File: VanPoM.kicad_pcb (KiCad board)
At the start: 2 copper layers, 5 parts, among them J1 Socket_ESP32-WROOM-32-NODEMCU, Q1 IPP055N03L G, Q2 IPP055N03L G, Q3 IPP120P04P4L03AKSA2, U1 BQ34Z100-R2

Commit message: +++ PCB; f many small things
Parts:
- added C1: 1000p, Capacitor_SMD:C_0603_1608Metric_Pad1.08x0.95mm_HandSolder, F.Cu at (140.3, 47.8)
- added C10: 1000p, Capacitor_SMD:C_0603_1608Metric_Pad1.08x0.95mm_HandSolder, F.Cu at (148.2, 53.1)
- added C11: 10u, Capacitor_SMD:C_1210_3225Metric_Pad1.33x2.70mm_HandSolder, F.Cu at (115.6, 70.0)
- added C12: 10u, Capacitor_SMD:C_1210_3225Metric_Pad1.33x2.70mm_HandSolder, F.Cu at (115.6, 74.3)
- added C13: 1000u, Capacitor_THT:CP_Radial_D16.0mm_P7.50mm, B.Cu at (115.8, 78.1)
- added C14: 0.1u, Capacitor_SMD:C_0603_1608Metric_Pad1.08x0.95mm_HandSolder, F.Cu at (109.3, 71.3)
- added C15: 1u, Capacitor_SMD:C_0402_1005Metric_Pad0.74x0.62mm_HandSolder, F.Cu at (111.3, 70.1)
- added C16: 0.1u, Capacitor_SMD:C_0603_1608Metric_Pad1.08x0.95mm_HandSolder, F.Cu at (105.2, 77.3)
- added C17: 0.1u, Capacitor_SMD:C_0603_1608Metric_Pad1.08x0.95mm_HandSolder, F.Cu at (173.4, 105.8)
- added C18: 0.1u, Capacitor_SMD:C_0603_1608Metric_Pad1.08x0.95mm_HandSolder, F.Cu at (173.4, 117.9)
- added C19: 1200u, Capacitor_THT:CP_Radial_D18.0mm_P7.50mm, B.Cu at (163.3, 89.8)
- added C2: 1u, Capacitor_SMD:C_0805_2012Metric_Pad1.18x1.45mm_HandSolder, F.Cu at (137.5, 96.9)
- added C20: 1200u, Capacitor_THT:CP_Radial_D18.0mm_P7.50mm, B.Cu at (178.7, 79.0)
- added C21: 0.1u, Capacitor_SMD:C_0603_1608Metric_Pad1.08x0.95mm_HandSolder, F.Cu at (173.4, 93.7)
- added C22: 4.7u, Capacitor_SMD:C_1206_3216Metric_Pad1.33x1.80mm_HandSolder, F.Cu at (179.7, 65.5)
- added C23: 4.7u, Capacitor_SMD:C_1206_3216Metric_Pad1.33x1.80mm_HandSolder, F.Cu at (179.7, 63.0)
- added C24: 4.7u, Capacitor_SMD:C_1206_3216Metric_Pad1.33x1.80mm_HandSolder, F.Cu at (179.7, 60.4)
- added C25: 4.7u, Capacitor_SMD:C_1206_3216Metric_Pad1.33x1.80mm_HandSolder, F.Cu at (179.7, 55.4)
- added C26: 4.7u, Capacitor_SMD:C_1206_3216Metric_Pad1.33x1.80mm_HandSolder, F.Cu at (179.7, 57.9)
- added C27: 10u, Capacitor_SMD:C_1210_3225Metric_Pad1.33x2.70mm_HandSolder, B.Cu at (177.5, 51.3)
- added C28: 0.022u, Capacitor_SMD:C_1206_3216Metric_Pad1.33x1.80mm_HandSolder, B.Cu at (187.9, 50.1)
- added C29: 50n, Capacitor_SMD:C_0402_1005Metric_Pad0.74x0.62mm_HandSolder, F.Cu at (185.4, 51.6)
- added C3: 220p, Capacitor_SMD:C_0603_1608Metric_Pad1.08x0.95mm_HandSolder, F.Cu at (142.9, 98.0)
- added C30: 10n, Capacitor_SMD:C_0402_1005Metric_Pad0.74x0.62mm_HandSolder, F.Cu at (183.2, 63.6)
- added C31: 1u, Capacitor_SMD:C_0805_2012Metric_Pad1.18x1.45mm_HandSolder, F.Cu at (143.2, 102.5)
- added C32: 1u, Capacitor_SMD:C_0402_1005Metric_Pad0.74x0.62mm_HandSolder, F.Cu at (143.9, 105.4)
- added C33: 0.1u, Capacitor_SMD:C_0603_1608Metric_Pad1.08x0.95mm_HandSolder, F.Cu at (180.4, 133.8)
- added C34: 0.1u, Capacitor_SMD:C_0603_1608Metric_Pad1.08x0.95mm_HandSolder, F.Cu at (128.5, 78.8)
- added C35: 0.1u, Capacitor_SMD:C_0603_1608Metric_Pad1.08x0.95mm_HandSolder, B.Cu at (109.3, 67.1)
- added C36: 0.1u, Capacitor_SMD:C_0603_1608Metric_Pad1.08x0.95mm_HandSolder, F.Cu at (137.9, 122.2)
- added C37: 0.1u, Capacitor_SMD:C_0603_1608Metric_Pad1.08x0.95mm_HandSolder, F.Cu at (145.0, 125.2)
- added C38: 0.1u, Capacitor_SMD:C_0603_1608Metric_Pad1.08x0.95mm_HandSolder, F.Cu at (148.1, 121.6)
- added C39: 0.1u, Capacitor_SMD:C_0603_1608Metric_Pad1.08x0.95mm_HandSolder, F.Cu at (147.5, 123.1)
- added C4: 560p, Capacitor_SMD:C_0402_1005Metric_Pad0.74x0.62mm_HandSolder, F.Cu at (140.0, 98.0)
- added C40: 0.1u, Capacitor_SMD:C_0603_1608Metric_Pad1.08x0.95mm_HandSolder, F.Cu at (141.6, 126.5)
- added C41: 0.1u, Capacitor_SMD:C_0603_1608Metric_Pad1.08x0.95mm_HandSolder, F.Cu at (140.1, 125.4)
- added C42: 0.1u, Capacitor_SMD:C_0603_1608Metric_Pad1.08x0.95mm_HandSolder, F.Cu at (136.4, 120.7)
- added C43: 0.1u, Capacitor_SMD:C_0603_1608Metric_Pad1.08x0.95mm_HandSolder, F.Cu at (143.1, 126.5)
- added C44: 1u, Capacitor_SMD:C_0402_1005Metric_Pad0.74x0.62mm_HandSolder, F.Cu at (143.5, 118.6)
- added C45: 1u, Capacitor_SMD:C_0402_1005Metric_Pad0.74x0.62mm_HandSolder, F.Cu at (145.2, 119.2)
- added C46: 1u, Capacitor_SMD:C_0402_1005Metric_Pad0.74x0.62mm_HandSolder, F.Cu at (147.0, 120.2)
- added C5: 0.1u, Capacitor_SMD:C_0603_1608Metric_Pad1.08x0.95mm_HandSolder, F.Cu at (140.6, 88.9)
- added C6: 0.1u, Capacitor_SMD:C_0603_1608Metric_Pad1.08x0.95mm_HandSolder, F.Cu at (150.7, 88.9)
- added C7: 560p, Capacitor_SMD:C_0402_1005Metric_Pad0.74x0.62mm_HandSolder, F.Cu at (149.0, 97.7)
- added C8: 220p, Capacitor_SMD:C_0603_1608Metric_Pad1.08x0.95mm_HandSolder, F.Cu at (151.9, 98.1)
- added C9: 1u, Capacitor_SMD:C_0805_2012Metric_Pad1.18x1.45mm_HandSolder, F.Cu at (146.5, 95.9)
- added D1: B1100-13-F, Diode_SMD:D_SMA, F.Cu at (142.7, 82.3)
- added D10: PESD2USB3UXT-QR, Package_TO_SOT_SMD:SOT-23-3, B.Cu at (105.8, 133.0)
- added D11: PESD2USB3UXT-QR, Package_TO_SOT_SMD:SOT-23-3, B.Cu at (105.9, 102.5)
- added D12: PESD2USB3UXT-QR, Package_TO_SOT_SMD:SOT-23-3, B.Cu at (105.8, 127.9)
- added D13: PESD2USB3UXT-QR, Package_TO_SOT_SMD:SOT-23-3, B.Cu at (105.9, 97.5)
- added D14: PESD2USB3UXT-QR, Package_TO_SOT_SMD:SOT-23-3, B.Cu at (105.9, 122.9)
- added D15: PESD2USB3UXT-QR, Package_TO_SOT_SMD:SOT-23-3, B.Cu at (105.8, 92.4)
- added D16: PESD2USB3UXT-QR, Package_TO_SOT_SMD:SOT-23-3, B.Cu at (105.8, 117.8)
- added D17: PESD2USB3UXT-QR, Package_TO_SOT_SMD:SOT-23-3, B.Cu at (105.9, 87.3)
- added D18: PESD2USB3UXT-QR, Package_TO_SOT_SMD:SOT-23-3, B.Cu at (105.8, 112.7)
- added D2: D, Diode_SMD:D_SMA, F.Cu at (136.6, 91.0)
- added D21: PESD2USB3UXT-QR, Package_TO_SOT_SMD:SOT-23-3, B.Cu at (110.0, 115.2)
- added D22: PESD2USB3UXT-QR, Package_TO_SOT_SMD:SOT-23-3, B.Cu at (110.0, 120.3)
- added D23: PESD2USB3UXT-QR, Package_TO_SOT_SMD:SOT-23-3, B.Cu at (110.0, 125.5)
- added D24: PESD2USB3UXT-QR, Package_TO_SOT_SMD:SOT-23-3, B.Cu at (110.0, 130.5)
- added D25: PESD2USB3UXT-QR, Package_TO_SOT_SMD:SOT-23-3, B.Cu at (110.0, 136.1)
- added D3: D, Diode_SMD:D_SMA, F.Cu at (146.3, 90.8)
- added D4: B1100-13-F, Diode_SMD:D_SMA, F.Cu at (150.6, 82.3)
- added D5: BZT52C15-7-F, Diode_SMD:D_SOD-123, F.Cu at (97.1, 71.6)
- added D6: PESD2USB3UXT-QR, Package_TO_SOT_SMD:SOT-23-3, B.Cu at (97.7, 78.2)
- added D7: PESD2USB3UXT-QR, Package_TO_SOT_SMD:SOT-23-3, B.Cu at (101.5, 79.1)
- added D8: PESD2USB3UXT-QR, Package_TO_SOT_SMD:SOT-23-3, B.Cu at (105.8, 138.1)
- added D9: PESD2USB3UXT-QR, Package_TO_SOT_SMD:SOT-23-3, B.Cu at (105.9, 107.6)
- added FB1: 74279201, Capacitor_SMD:C_0805_2012Metric_Pad1.18x1.45mm_HandSolder, F.Cu at (180.4, 137.7)
- added FB2: 74279201, Capacitor_SMD:C_0805_2012Metric_Pad1.18x1.45mm_HandSolder, F.Cu at (132.5, 78.8)
- added FB3: 74279201, Capacitor_SMD:C_0805_2012Metric_Pad1.18x1.45mm_HandSolder, B.Cu at (111.2, 68.8)
- added IC1: UCC27517DBVR, Perso:SOT95P280X145-5N, F.Cu at (105.2, 74.4)
- added IC2: TLV70433DBVT, Perso:SOT95P280X145-5N, F.Cu at (147.3, 104.1)
- added IC3: SN74LV4052APWR, Package_SO:TSSOP-16_4.4x5mm_P0.65mm, F.Cu at (119.0, 133.3)
- added J10: UART1, Connector_PinHeader_2.54mm:PinHeader_1x04_P2.54mm_Vertical, B.Cu at (121.5, 128.3)
- added J11: I2C, Connector_PinHeader_2.54mm:PinHeader_1x04_P2.54mm_Vertical, B.Cu at (121.5, 138.0)
- added J2: OSTT7020150, TerminalBlock_MetzConnect:TerminalBlock_MetzConnect_Type073_RT02602HBLU_1x02_P5.08mm_Horizontal, B.Cu at (185.6, 123.8)
- added J3: OSTT7020150, TerminalBlock_MetzConnect:TerminalBlock_MetzConnect_Type073_RT02602HBLU_1x02_P5.08mm_Horizontal, B.Cu at (185.6, 99.7)
- added J4: OSTT7020150, TerminalBlock_MetzConnect:TerminalBlock_MetzConnect_Type073_RT02602HBLU_1x02_P5.08mm_Horizontal, B.Cu at (110.1, 51.4)
- added J5: OSTT7020150, TerminalBlock_MetzConnect:TerminalBlock_MetzConnect_Type073_RT02602HBLU_1x02_P5.08mm_Horizontal, B.Cu at (98.0, 51.4)
- added J6: Conn_03x23_Row_Letter_First, Perso:PinHeader_3x23_P2.54mm_Vertical, B.Cu at (101.8, 83.2)
- added J7: UART4, Connector_PinHeader_2.54mm:PinHeader_1x04_P2.54mm_Vertical, B.Cu at (121.5, 111.1)
- added J8: UART3, Connector_PinHeader_2.54mm:PinHeader_1x04_P2.54mm_Vertical, B.Cu at (121.5, 116.8)
- added J9: UART2, Connector_PinHeader_2.54mm:PinHeader_1x04_P2.54mm_Vertical, B.Cu at (121.5, 122.5)
- added L1: 22u, Inductor_SMD:L_Wuerth_HCF-2818, F.Cu at (128.7, 62.9)
- added L2: 22u, Inductor_SMD:L_Wuerth_HCF-2818, F.Cu at (166.6, 62.9)
- added L3: 220u, Perso:INDPM105103X500N, B.Cu at (185.4, 58.7)
- added Q10: CSD18540Q5B, Package_SON:VSONP-8-1EP_5x6_P1.27mm, F.Cu at (167.4, 123.2)
- added Q11: CSD18540Q5B, Package_SON:VSONP-8-1EP_5x6_P1.27mm, F.Cu at (167.4, 99.1)
- added Q4: CSD19531Q5A, Package_SON:VSONP-8-1EP_5x6_P1.27mm, F.Cu at (152.8, 76.7)
- added Q5: NX7002AK,215, Package_TO_SOT_SMD:SOT-23-3, F.Cu at (115.3, 63.4)
- added Q6: BSS84W-7-F, Package_TO_SOT_SMD:SOT-323_SC-70_Handsoldering, F.Cu at (114.7, 57.2)
- added Q7: CSD18540Q5B, Package_SON:VSONP-8-1EP_5x6_P1.27mm, F.Cu at (101.9, 67.9)
- added Q8: CSD18540Q5B, Package_SON:VSONP-8-1EP_5x6_P1.27mm, F.Cu at (98.4, 57.1)
- added Q9: CSD18540Q5B, Package_SON:VSONP-8-1EP_5x6_P1.27mm, F.Cu at (167.4, 111.1)
- added R1: 5.6, Resistor_SMD:R_0805_2012Metric_Pad1.20x1.40mm_HandSolder, F.Cu at (140.1, 51.8)
- added R10: 330k, Resistor_SMD:R_0805_2012Metric_Pad1.20x1.40mm_HandSolder, F.Cu at (115.4, 60.3)
- added R11: 390k, Resistor_SMD:R_0805_2012Metric_Pad1.20x1.40mm_HandSolder, F.Cu at (112.1, 63.6)
- added R12: 30k, Resistor_SMD:R_0805_2012Metric_Pad1.20x1.40mm_HandSolder, F.Cu at (112.1, 67.4)
- added R13: 10k, Resistor_SMD:R_0805_2012Metric_Pad1.20x1.40mm_HandSolder, F.Cu at (98.1, 75.3)
- added R14: 5.11, Resistor_SMD:R_0805_2012Metric_Pad1.20x1.40mm_HandSolder, F.Cu at (101.4, 73.2)
- added R15: 100k, Resistor_SMD:R_0805_2012Metric_Pad1.20x1.40mm_HandSolder, F.Cu at (176.1, 105.7)
- added R16: 100k, Resistor_SMD:R_0805_2012Metric_Pad1.20x1.40mm_HandSolder, F.Cu at (176.1, 117.7)
- added R17: 140k, Resistor_SMD:R_0805_2012Metric_Pad1.20x1.40mm_HandSolder, B.Cu at (177.0, 47.4)
- added R18: 220k, Resistor_SMD:R_0805_2012Metric_Pad1.20x1.40mm_HandSolder, F.Cu at (183.6, 56.4)
- added R19: 30k, Resistor_SMD:R_0805_2012Metric_Pad1.20x1.40mm_HandSolder, F.Cu at (182.6, 53.1)
- added R2: 4.42, Resistor_SMD:R_0805_2012Metric_Pad1.20x1.40mm_HandSolder, F.Cu at (142.8, 86.1)
- added R20: 3.00, Resistor_SMD:R_0805_2012Metric_Pad1.20x1.40mm_HandSolder, F.Cu at (183.6, 60.6)
- added R21: 10k, Resistor_SMD:R_0805_2012Metric_Pad1.20x1.40mm_HandSolder, F.Cu at (139.1, 114.7)
- added R22: 10k, Resistor_SMD:R_0805_2012Metric_Pad1.20x1.40mm_HandSolder, F.Cu at (139.1, 116.8)
- added R23: 100k, Resistor_SMD:R_0805_2012Metric_Pad1.20x1.40mm_HandSolder, F.Cu at (152.4, 138.9)
- added R24: 1.8M, Resistor_SMD:R_0805_2012Metric_Pad1.20x1.40mm_HandSolder, F.Cu at (148.9, 128.0)
- added R25: 1.8M, Resistor_SMD:R_0805_2012Metric_Pad1.20x1.40mm_HandSolder, F.Cu at (150.8, 120.9)
- added R26: 1.8M, Resistor_SMD:R_0805_2012Metric_Pad1.20x1.40mm_HandSolder, F.Cu at (146.9, 131.1)
- added R27: 1.8M, Resistor_SMD:R_0805_2012Metric_Pad1.20x1.40mm_HandSolder, F.Cu at (137.1, 125.4)
- added R28: 200k, Resistor_SMD:R_0805_2012Metric_Pad1.20x1.40mm_HandSolder, F.Cu at (135.2, 123.4)
- added R29: 200k, Resistor_SMD:R_0805_2012Metric_Pad1.20x1.40mm_HandSolder, F.Cu at (146.1, 128.0)
- added R3: 2.21, Resistor_SMD:R_0805_2012Metric_Pad1.20x1.40mm_HandSolder, F.Cu at (140.6, 73.7)
- added R30: 200k, Resistor_SMD:R_0805_2012Metric_Pad1.20x1.40mm_HandSolder, F.Cu at (150.8, 117.1)
- added R31: 200k, Resistor_SMD:R_0805_2012Metric_Pad1.20x1.40mm_HandSolder, F.Cu at (149.7, 125.0)
- added R32: R, Resistor_SMD:R_0805_2012Metric_Pad1.20x1.40mm_HandSolder, F.Cu at (146.9, 117.6)
- added R33: R, Resistor_SMD:R_0805_2012Metric_Pad1.20x1.40mm_HandSolder, F.Cu at (143.1, 117.1)
- added R34: 100k, Resistor_SMD:R_0805_2012Metric_Pad1.20x1.40mm_HandSolder, B.Cu at (117.6, 125.3)
- added R35: 100k, Resistor_SMD:R_0805_2012Metric_Pad1.20x1.40mm_HandSolder, B.Cu at (117.7, 113.9)
- added R36: 100k, Resistor_SMD:R_0805_2012Metric_Pad1.20x1.40mm_HandSolder, B.Cu at (117.7, 108.2)
- added R37: 100k, Resistor_SMD:R_0805_2012Metric_Pad1.20x1.40mm_HandSolder, B.Cu at (117.6, 119.6)
- added R4: 2.21, Resistor_SMD:R_0805_2012Metric_Pad1.20x1.40mm_HandSolder, F.Cu at (146.8, 62.7)
- added R5: 2.21, Resistor_SMD:R_0805_2012Metric_Pad1.20x1.40mm_HandSolder, F.Cu at (158.6, 82.8)
- added R6: 2.21, Resistor_SMD:R_0805_2012Metric_Pad1.20x1.40mm_HandSolder, F.Cu at (148.9, 73.6)
- added R7: 4.42, Resistor_SMD:R_0805_2012Metric_Pad1.20x1.40mm_HandSolder, F.Cu at (152.8, 86.2)
- added R8: 5.6, Resistor_SMD:R_0805_2012Metric_Pad1.20x1.40mm_HandSolder, F.Cu at (148.1, 56.9)
- added R9: 240k, Resistor_SMD:R_0805_2012Metric_Pad1.20x1.40mm_HandSolder, F.Cu at (115.7, 54.5)
- added R_sense1: 2m, Perso:R_Shunt_Ohmite_LVK25-fixed, F.Cu at (120.9, 84.2)
- added R_sense2: 2m, Perso:R_Shunt_Ohmite_LVK25-fixed, F.Cu at (109.3, 57.3)
- added R_sense3: 2m, Perso:R_Shunt_Ohmite_LVK25-fixed, F.Cu at (175.3, 126.2)
- added U10: LM5163DDAR, Perso:SOIC-8-1EP_3.9x4.9mm_P1.27mm_EP2.34x2.34mm_ThermalVias, B.Cu at (182.9, 49.7)
- added U11: TVS3300DRV, Package_SON:WSON-6-1EP_2x2mm_P0.65mm_EP1x1.6mm, B.Cu at (103.3, 58.9)
- added U12: TVS3300DRV, Package_SON:WSON-6-1EP_2x2mm_P0.65mm_EP1x1.6mm, B.Cu at (121.1, 49.7)
- added U13: ESP32-S3-DEVKITC-1-N16R2, Perso:XCVR_ESP32-S3-DEVKITC-1, B.Cu at (144.4, 110.4)
- added U14: INA240A2D, Package_SO:SOIC-8_3.9x4.9mm_P1.27mm, F.Cu at (175.4, 133.9)
- added U15: INA240A2D, Package_SO:SOIC-8_3.9x4.9mm_P1.27mm, F.Cu at (128.6, 84.2)
- added U16: INA240A2D, Package_SO:SOIC-8_3.9x4.9mm_P1.27mm, B.Cu at (109.3, 63.6)
- added U17: TLA2528IRTER, Perso:WQFN16_RTE_TEX-L, F.Cu at (142.6, 121.0)
- added U18: TVS3300DRV, Package_SON:WSON-6-1EP_2x2mm_P0.65mm_EP1x1.6mm, B.Cu at (98.9, 58.9)
- added U2: LM5109BMA/NOPB, Package_SO:SOIC-8_3.9x4.9mm_P1.27mm, F.Cu at (151.4, 93.3)
- added U3: BQ34Z100-R2, Package_SO:TSSOP-14_4.4x5mm_P0.65mm, F.Cu at (108.3, 65.7)
- added U4: TVS3300DRV, Package_SON:WSON-6-1EP_2x2mm_P0.65mm_EP1x1.6mm, B.Cu at (178.3, 111.7)
- added U5: TVS3300DRV, Package_SON:WSON-6-1EP_2x2mm_P0.65mm_EP1x1.6mm, B.Cu at (178.3, 123.8)
- added U6: LM74700, Package_TO_SOT_SMD:SOT-23-6, F.Cu at (170.3, 105.5)
- added U7: LM74700, Package_TO_SOT_SMD:SOT-23-6, F.Cu at (170.3, 117.6)
- added U8: LM74700, Package_TO_SOT_SMD:SOT-23-6, F.Cu at (170.3, 93.5)
- added U9: TVS3300DRV, Package_SON:WSON-6-1EP_2x2mm_P0.65mm_EP1x1.6mm, B.Cu at (185.8, 95.2)
- J1: value Socket_ESP32-WROOM-32-NODEMCU -> OSTT7020150; footprint Connector_PinSocket_2.54mm:PinSocket_1x19_P2.54mm_Vertical -> TerminalBlock_MetzConnect:TerminalBlock_MetzConnect_Type073_RT02602HBLU_1x02_P5.08mm_Horizontal; moved to B.Cu
- Q1, Q2: value IPP055N03L G -> CSD19531Q5A; footprint Package_TO_SOT_THT:TO-220-3_Vertical -> Package_SON:VSONP-8-1EP_5x6_P1.27mm
- Q3: value IPP120P04P4L03AKSA2 -> CSD19531Q5A; footprint Package_TO_SOT_THT:TO-220-3_Vertical -> Package_SON:VSONP-8-1EP_5x6_P1.27mm
- U1: value BQ34Z100-R2 -> LM5109BMA/NOPB; footprint Package_SO:TSSOP-14_4.4x5mm_P0.65mm -> Package_SO:SOIC-8_3.9x4.9mm_P1.27mm
- moved J1 67.3 mm to (185.6, 111.8), turned to -90 degrees
- moved Q3 52.7 mm to (152.7, 49.8), turned to 90 degrees
- moved Q2 44.0 mm to (144.3, 49.8), turned to 90 degrees
- moved Q1 17.3 mm to (144.9, 76.7), turned to 90 degrees
- moved U1 13.7 mm to (141.2, 93.3), turned to 90 degrees
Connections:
- J1 pad 1: unconnected-(J1-5V-Pad1) -> V_S
- J1 pad 2: unconnected-(J1-CLK-Pad2) -> P-
- Q1 pad 1: Net-(D1-K) -> P-
- Q1 pad 2: BAT + -> Net-(Q1-S-Pad2)
- Q1 pad 3: (no net) -> Net-(L1-Pad2)
- Q2 pad 1: BAT - -> Net-(L1-Pad2)
- Q2 pad 3: (no net) -> V_IN
- Q3 pad 3: BAT + -> V_IN
- U1 pad 1: BAT - -> +10V
- U1 pad 2: Net-(Q2-G) -> PW_H1
- U1 pad 3: BAT - -> PW_L1
- U1 pad 4: Net-(U1-BAT) -> P-
- U1 pad 5: Net-(Q1-3) -> Net-(U1-LO)
- U1 pad 6: Net-(Q1-3) -> Net-(D1-K)
- U1 pad 7: unconnected-(U1-REG25-Pad7) -> Net-(U1-HO)
- U1 pad 8: BAT - -> Net-(D2-K)
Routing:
- net P-: track 0.00 -> 606.7 mm, vias 0 -> 189
- net +3V3: track 0.00 -> 372.3 mm, vias 0 -> 8
- net TVS: track 0.00 -> 222.3 mm, vias 0 -> 2
- net 103AT: track 0.00 -> 158.9 mm
- net +10V: track 0.00 -> 146.1 mm, vias 0 -> 8
- net SCL: track 0.00 -> 139.4 mm, vias 0 -> 5
- net SDA: track 0.00 -> 132.7 mm, vias 0 -> 2
- net GPIO19: track 0.00 -> 93.1 mm
- net AIO_2: track 0.00 -> 91.1 mm, vias 0 -> 3
- net GPIO39: track 0.00 -> 88.7 mm, vias 0 -> 2
- net GPIO20: track 0.00 -> 87.1 mm
- net GPIO40: track 0.00 -> 86.8 mm, vias 0 -> 2
- net TVS_3v3: track 0.00 -> 86.3 mm
- net GPIO1: track 0.00 -> 86.2 mm, vias 0 -> 2
- net GPIO41: track 0.00 -> 85.7 mm, vias 0 -> 2
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- added copper zone on F.Cu, net +10V
- added copper zone on F.Cu, net +3V3
- added copper zone on B.Cu, net BAT+
- added copper zone on F.Cu, net BAT+
- added copper zone on F.Cu, net BAT-
- added copper zone on F.Cu, net Net-(C11-Pad1)
- added copper zone on F.Cu, net Net-(D2-K)
- added copper zone on F.Cu, net Net-(D3-K)
- added copper zone on B.Cu, net Net-(L1-Pad2)
- added copper zone on F.Cu, net Net-(L1-Pad2)
- added copper zone on B.Cu, net Net-(L2-Pad1)
- added copper zone on F.Cu, net Net-(L2-Pad1)
- added copper zone on F.Cu, net Net-(Q7-S-Pad3)
- added copper zone on B.Cu, net Net-(U10-SW)
- added copper zone on B.Cu, net OUT-
- added copper zone on F.Cu, net OUT-
- added copper zone on B.Cu, net P+
- added copper zone on F.Cu, net P+
- added copper zone on B.Cu, net P-
- added copper zone on F.Cu, net P-
- added copper zone on B.Cu, net V_A
- added copper zone on F.Cu, net V_A
- added copper zone on B.Cu, net V_IN
- added copper zone on F.Cu, net V_IN
- added copper zone on F.Cu, net V_P
- added copper zone on B.Cu, net V_S
- added copper zone on F.Cu, net V_S
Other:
- board outline added: 97 x 97 mm
- board text added: "+"
- board text added: "+15V INPUT (FROM AC/DC CONVERTER)"
- board text added: "00"
- board text added: "01"
- board text added: "02"
- board text added: "03"
- board text added: "06"
- board text added: "07"
- board text added: "08"
- board text added: "15"
- board text added: "16"
- board text added: "17"
- board text added: "18"
- board text added: "19"
- board text added: "20"
- board text added: "21"
- board text added: "39"
- board text added: "3V3"
- board text added: "40"
- board text added: "41"
- board text added: "42"
- board text added: "45"
- board text added: "46"
- board text added: "47"
- board text added: "48"
- board text added: "BAT TEMP"
- board text added: "BATTERY"
- board text added: "CAR BATTERY"
- board text added: "GND"
- board text added: "I2C"
- board text added: "IO"
- board text added: "LOAD"
- board text added: "RX"
- board text added: "SCL"
- board text added: "SDA"
- board text added: "SOLAR PANELS"
- board text added: "TX"
- board text added: "UART1"
- board text added: "UART2"
- board text added: "UART3"
- board text added: "UART4"
- board text added: "VanPom v1.0 Copyright © Léo Flaventin Hauchecorne https://github.com/hl037/VanPom"
- board text added: "−"

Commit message: + screen shots
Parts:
- moved C10 72.6 mm to (77.7, 36.0)
- moved C37 72.6 mm to (74.4, 108.1)
- moved C41 72.6 mm to (69.5, 108.4)
- moved C43 72.6 mm to (72.6, 109.4)
- moved C9 72.6 mm to (76.0, 78.8)
- moved L3 72.6 mm to (114.8, 41.6)
- moved R21 72.6 mm to (68.5, 97.6)
- moved R22 72.6 mm to (68.5, 99.7)
- moved R26 72.6 mm to (76.4, 114.0)
- moved R32 72.6 mm to (76.4, 100.5)
- moved R5 72.6 mm to (88.0, 65.7)
- moved U1 72.6 mm to (70.6, 76.3)
- moved U6 72.6 mm to (99.7, 88.4)
- moved U7 72.6 mm to (99.7, 100.5)
- moved U8 72.6 mm to (99.7, 76.4)
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
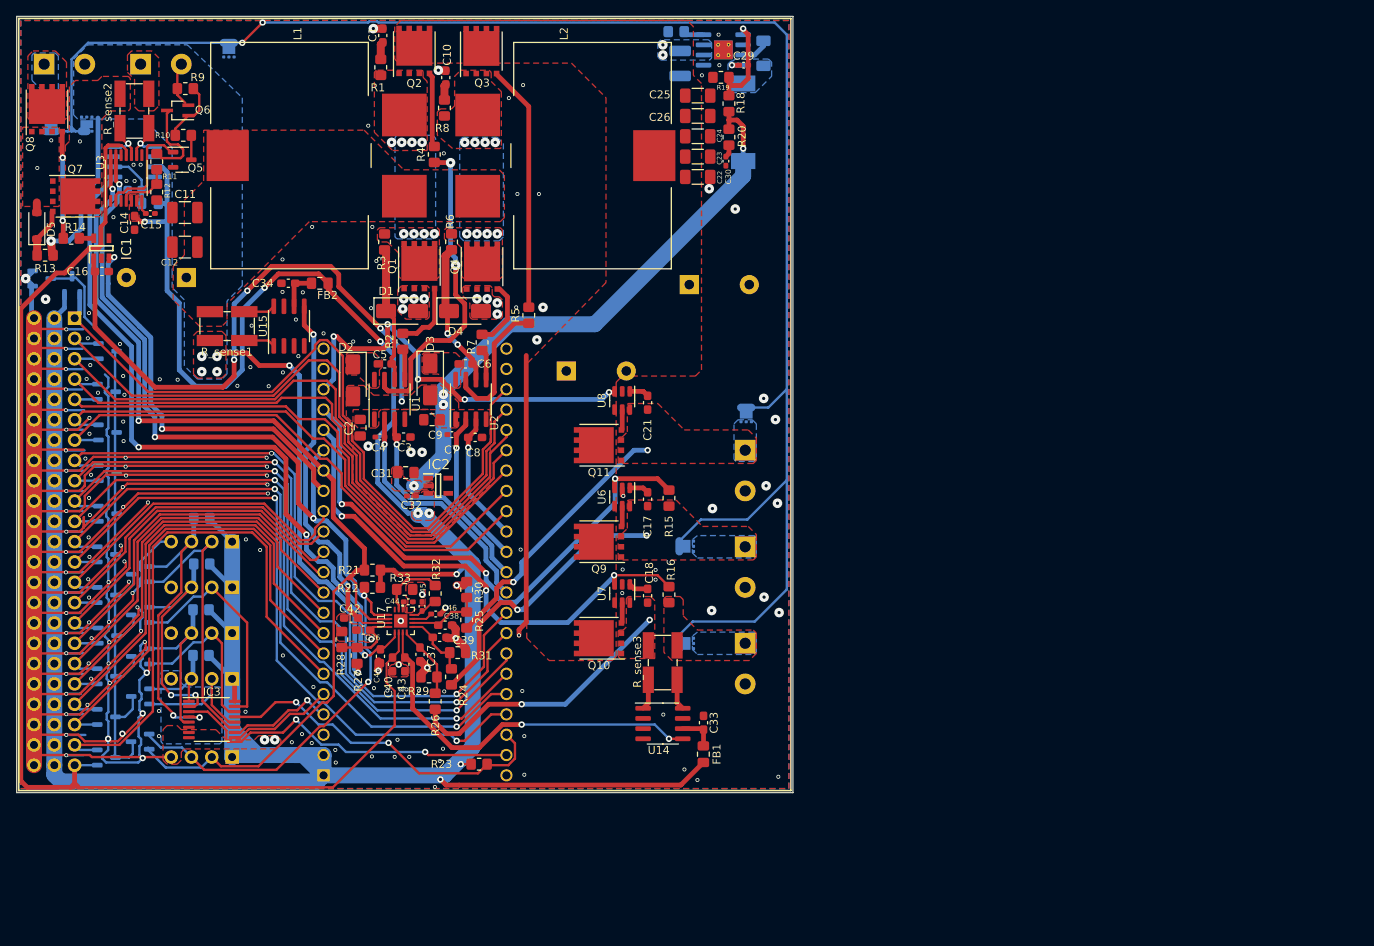
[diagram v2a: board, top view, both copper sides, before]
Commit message: + Thermal reliefs
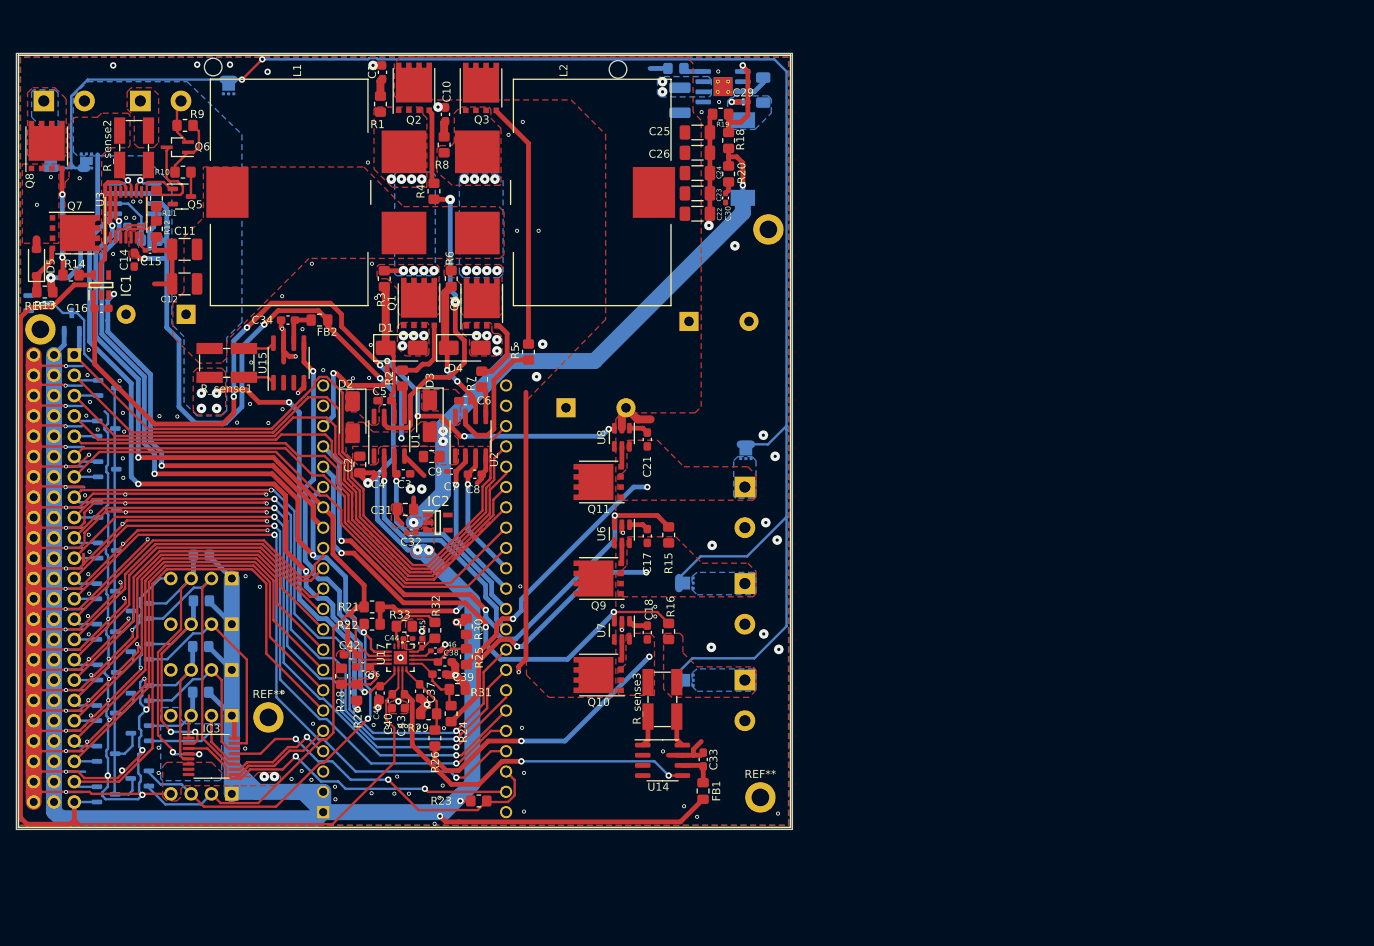
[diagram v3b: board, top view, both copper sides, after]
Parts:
- added ?: , , F.Cu at (118.0, 55.0)
- added REF**: MountingHole_2.2mm_M2_DIN965_Pad, MountingHole:MountingHole_2.2mm_M2_DIN965_Pad, F.Cu at (117.0, 126.0)
- added REF**: MountingHole_2.2mm_M2_DIN965_Pad, MountingHole:MountingHole_2.2mm_M2_DIN965_Pad, F.Cu at (55.5, 116.0)
- added REF**: MountingHole_2.2mm_M2_DIN965_Pad, MountingHole:MountingHole_2.2mm_M2_DIN965_Pad, F.Cu at (27.0, 67.5)
- moved D7 4.60 mm to (30.9, 66.6)
- moved Q4 4.60 mm to (82.2, 64.2)
- moved C1 4.60 mm to (69.8, 35.4)
- moved C12 4.60 mm to (45.0, 61.8)
- moved C13 4.60 mm to (45.2, 65.6)
- moved C14 4.60 mm to (38.7, 58.8)
- moved C15 4.60 mm to (40.7, 57.6)
- moved C16 4.60 mm to (34.6, 64.9)
- moved C17 4.60 mm to (102.9, 93.3)
- moved C19 4.60 mm to (92.7, 77.3)
- moved C20 4.60 mm to (108.1, 66.5)
- moved C21 4.60 mm to (102.9, 81.3)
- moved C23 4.60 mm to (109.1, 50.5)
- moved C24 4.60 mm to (109.1, 48.0)
- moved C25 4.60 mm to (109.1, 42.9)
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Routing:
- net P-: track 606.7 -> 675.0 mm, vias 189 -> 190
- net Net-(L1-Pad2): track 0.00 -> 2.41 mm
- net +10V: track 146.1 -> 148.1 mm
- net 103AT: track 158.9 -> 161.0 mm
- net TVS_3v3: track 86.3 -> 87.5 mm
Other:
- outline, holes or cut-outs redrawn
